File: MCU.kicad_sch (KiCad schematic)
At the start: 34 parts, among them J1 USB4105-GF-A, J2 USB4105-GF-A, Q2 2N7002-TP, Q3 2N7002-TP, U4 ESP32-S3-WROOM-1-N8, U5 FT231XS

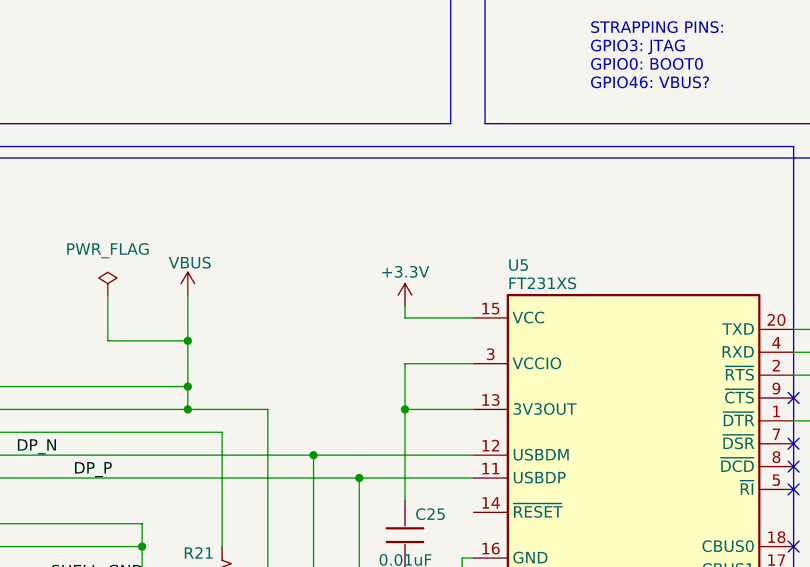
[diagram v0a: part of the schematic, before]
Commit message: Updated schematics/ pcb
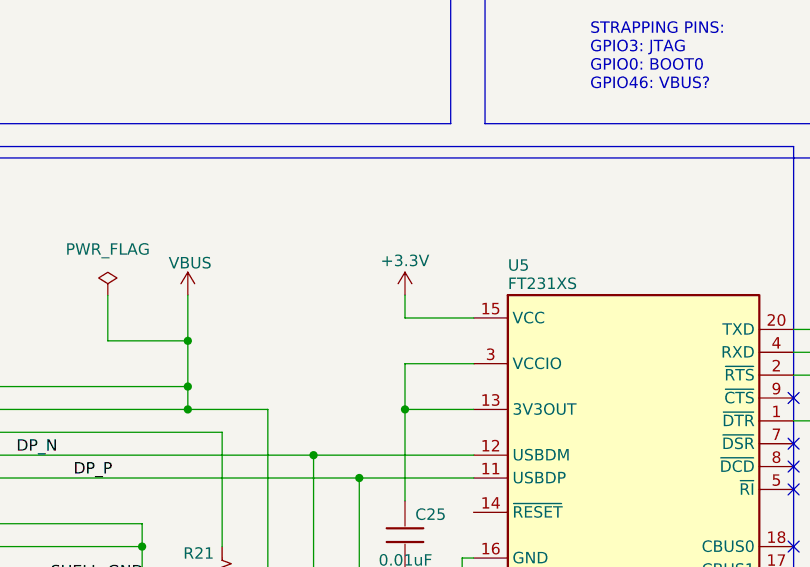
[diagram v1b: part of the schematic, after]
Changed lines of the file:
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@@
 	(wire
 		(pts
-			(xy 121.92 128.27) (xy 121.92 129.54)
+			(xy 121.92 127) (xy 121.92 129.54)
 		)
 		(stroke
@@
 	(symbol
 		(lib_id "power:+5V")
-		(at 121.92 128.27 0)
+		(at 121.92 127 0)
 		(unit 1)
 		(exclude_from_sim no)
@@
 		(dnp no)
 		(property "Reference" "#PWR028"
-			(at 121.92 132.08 0)
+			(at 121.92 130.81 0)
 			(effects
 				(font
@@
 		)
 		(property "Value" "+3.3V"
-			(at 121.92 124.46 0)
+			(at 121.92 123.19 0)
 			(effects
 				(font
@@
 		)
 		(property "Footprint" ""
-			(at 121.92 128.27 0)
+			(at 121.92 127 0)
 			(effects
 				(font
@@
 		)
 		(property "Datasheet" ""
-			(at 121.92 128.27 0)
+			(at 121.92 127 0)
 			(effects
 				(font
@@
 		)
 		(property "Description" "Power symbol creates a global label with name \"+5V\""
-			(at 121.92 128.27 0)
+			(at 121.92 127 0)
 			(effects
 				(font
@@
 		)
 		(property "MPN" ""
-			(at 121.92 128.27 0)
+			(at 121.92 127 0)
 			(effects
 				(font

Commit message: revisions after design review by Ted Yapo
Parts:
- added R25, R26, R27: 33R, Resistor_SMD:R_0805_2012Metric, symbol Device:R_US
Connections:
- net I2S_BCK: now also R25.1; no longer U4.28 (IO35)
- net I2S_DOUT: now also R27.1; no longer U4.30 (IO37)
- net I2S_LRCK: now also R26.1; no longer U4.29 (IO36)
- new net: R25.2, U4.28 (IO35)
- new net: R26.2, U4.29 (IO36)
- new net: R27.2, U4.30 (IO37)
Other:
- moved on the sheet: C10, C9, R10, R11

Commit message: proto 1 final
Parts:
- J1, J2: footprint GCT_USB4105-GF-A -> USB4105-GF-A:GCT_USB4105-GF-A
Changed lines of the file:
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@@
 			)
 		)
-		(property "Footprint" "GCT_USB4105-GF-A"
+		(property "Footprint" "USB4105-GF-A:GCT_USB4105-GF-A"
 			(at 52.07 48.26 0)
 			(effects
@@
 			)
 		)
-		(property "Footprint" "GCT_USB4105-GF-A"
+		(property "Footprint" "USB4105-GF-A:GCT_USB4105-GF-A"
 			(at 54.61 147.32 0)
 			(effects
